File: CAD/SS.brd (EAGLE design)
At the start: 77 x 109 mm, 82 parts, among them Q1 SN74AHC-OR, Q2 UMD5N, Q4 SN74AHC-OR, Q5 BFP460, Q6 L78L05, Q7 NCP553, T1 MMBTRA104SS

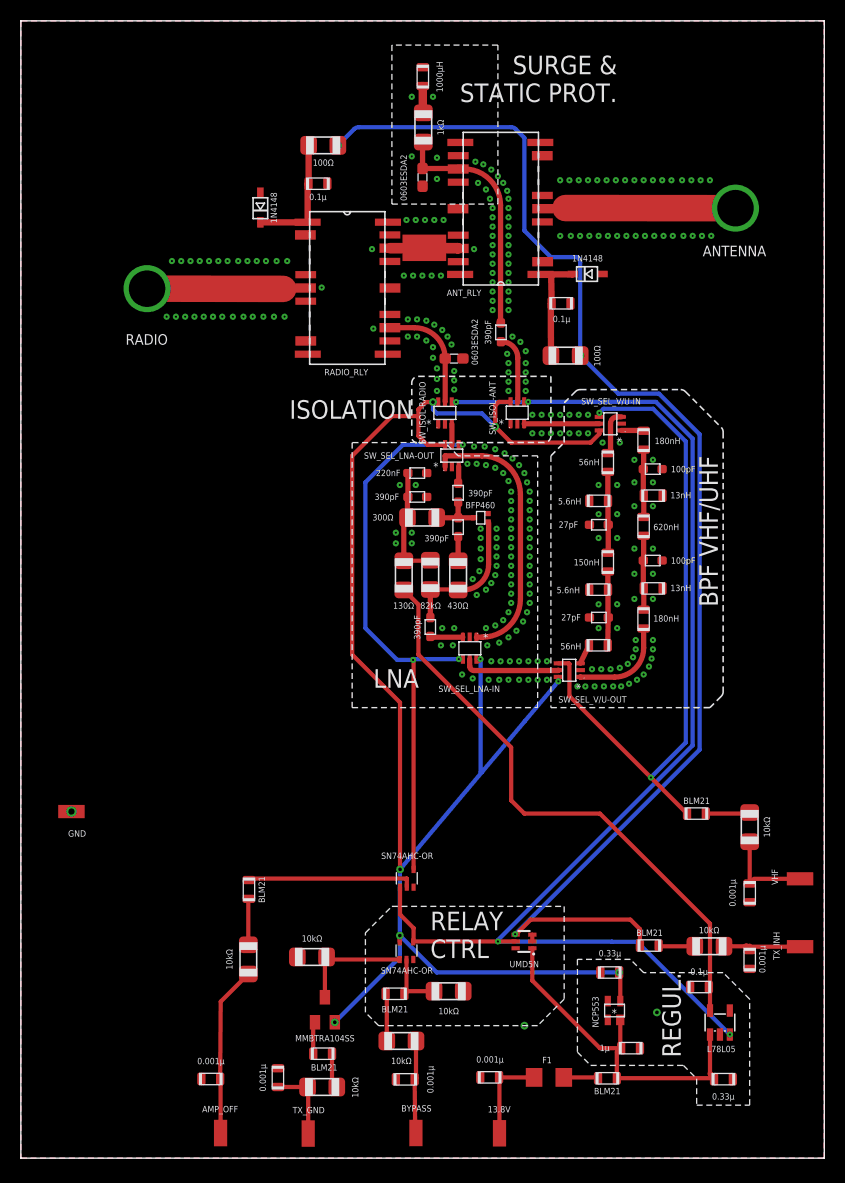
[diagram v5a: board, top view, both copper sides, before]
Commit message: Fixed relay/switch logics
* REviewed thoroughly the relay logic and connectors.
* Had to add a new "NOR" part. Complexity wins...
* Re-routed 5V regulator Enable pin to LNA logic
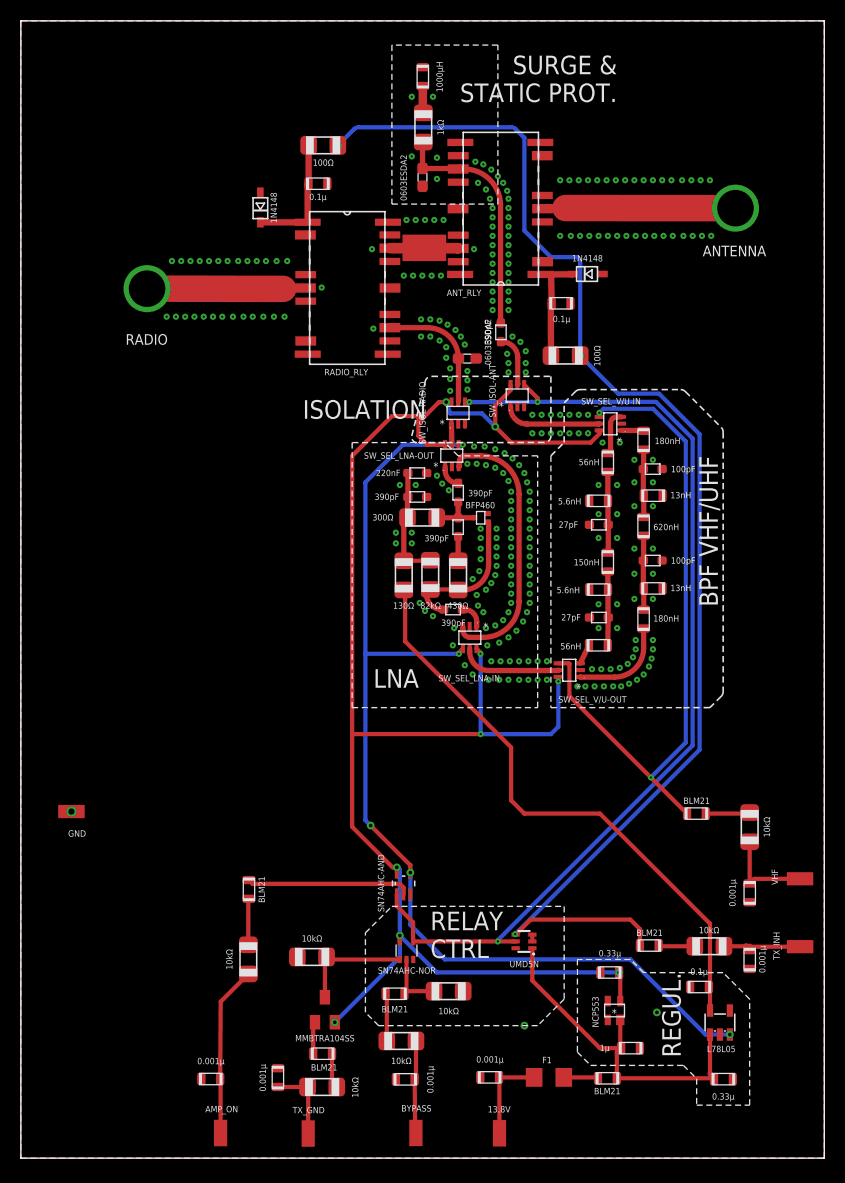
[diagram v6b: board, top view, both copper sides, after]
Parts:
- AMP_ON: value AMP_OFF -> AMP_ON
- Q1: value SN74AHC-OR -> SN74AHC-NOR
- Q4: value SN74AHC-OR -> SN74AHC-AND; device aarf:SC70-5 -> aarf:DCK5
- moved C8 2.75 mm to (41.4, 52.6), turned to 180 degrees
- moved SW_ISOL-ANT 1.65 mm to (47.6, 73.1)
- moved SW_ISOL-RADIO 1.27 mm to (41.9, 71.4)
- moved D4 1.27 mm to (42.8, 76.6)
- moved SW_SEL_LNA-IN 1.02 mm to (43.0, 49.9)
- moved Q4 0.59 mm to (36.7, 26.3), turned to 90 degrees
- renumbered AMP_OFF to AMP_ON
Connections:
- net AMP_OFF renamed AMP_ON
- net EXT_BYPASS renamed FORCE_BYPASS
- net RELAY_PWR renamed RELAY-RX_ON
- removed net LNA_OFF: Q4.4, SW_SEL_LNA-IN.4, SW_SEL_LNA-OUT.4
- removed net N$4: C8.P$1, SW_SEL_LNA-IN.3
- removed net RLY_BYPASS: Q1.4, Q2.5, Q4.1, Q6.3, SW_ISOL-ANT.4, SW_ISOL-RADIO.4
- new net BPF_ON: Q1.4, Q2.5, Q4.1, SW_ISOL-ANT.4, SW_ISOL-RADIO.4
- new net LNA_ON: Q4.4, Q6.3, SW_SEL_LNA-IN.4, SW_SEL_LNA-OUT.4
- new net N$3: C8.P$1, SW_SEL_LNA-IN.1
- net BPF_IN: now also SW_ISOL-ANT.1; no longer SW_ISOL-ANT.3
- net GND: now also SW_ISOL-ANT.3, SW_ISOL-RADIO.3; no longer SW_ISOL-ANT.1, SW_ISOL-RADIO.1
- net LNA-BYPASS: now also SW_SEL_LNA-IN.3, SW_SEL_LNA-OUT.3; no longer SW_SEL_LNA-IN.1, SW_SEL_LNA-OUT.1
- net LNA-SW_OUT: now also SW_ISOL-RADIO.1; no longer SW_ISOL-RADIO.3
- net N$1: now also SW_SEL_LNA-OUT.1; no longer SW_SEL_LNA-OUT.3
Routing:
- net RLY_BYPASS: track 122.5 -> 0.00 mm, vias 4 -> 0
- net LNA_ON: track 0.00 -> 100.0 mm, vias 0 -> 5
- net BPF_ON: track 0.00 -> 96.6 mm, vias 0 -> 3
- net LNA_OFF: track 55.9 -> 0.00 mm, vias 3 -> 0
- net N$4: track 3.15 -> 0.00 mm
- net N$3: track 0.00 -> 2.33 mm
- net BPF_IN: track 7.22 -> 9.28 mm
- net IN_DECPL: track 6.50 -> 4.84 mm
- net AMP+BPF_OUT: track 10.7 -> 12.0 mm
- net 3V: track 158.1 -> 157.3 mm, vias 8 -> 9
- net GND: track 0.13 -> 0.00 mm, vias 296 -> 298

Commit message: Updates to Board & Schematics
Schematic: 
* Added pads for 3V and 5V
Board:
* Added signal direction on signal pads
* Added a lot of gimmicks
* Added exposed copper so I can try the effects of covering some RF-critical sections with copper tape
* Reviewed some component position
* More comments
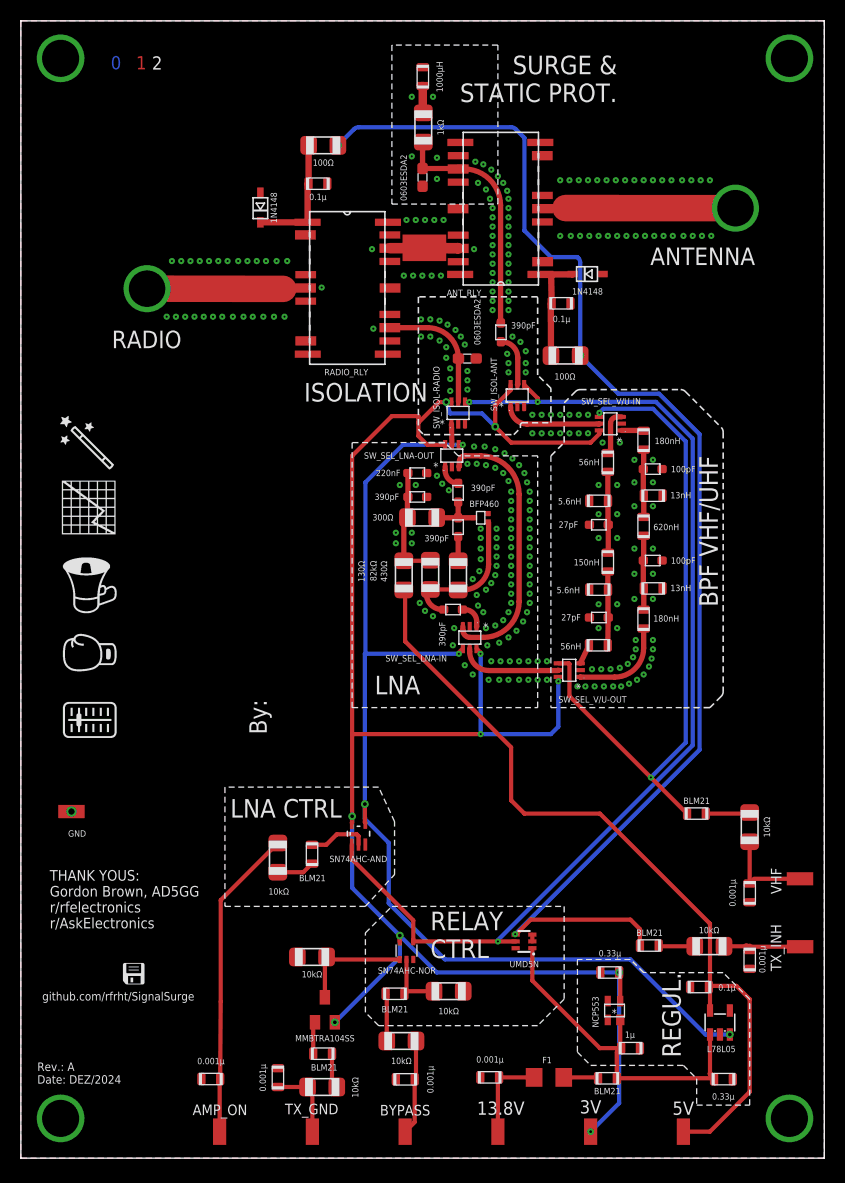
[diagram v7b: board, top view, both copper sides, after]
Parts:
- added 3V: 3V, wirepad:SMD1,27-2,54
- added 5V: 5V, wirepad:SMD1,27-2,54
- moved R12 10.2 mm to (24.6, 28.8), turned to 90 degrees
- moved FB6 6.93 mm to (27.9, 29.1)
- moved Q4 6.44 mm to (32.4, 31.1)
- moved BYPASS 1.04 mm to (36.8, 2.54)
- moved TX_GND 0.44 mm to (27.9, 2.54)
- moved 13.8V 0.22 mm to (45.7, 2.54)
- moved AMP_ON 0.16 mm to (19.1, 2.54)
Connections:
- net 3V: now also 3V.1
- net 5V: now also 5V.1
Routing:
- net 5V: track 56.8 -> 78.1 mm
- net 3V: track 157.3 -> 173.6 mm, vias 9 -> 10
- net N$15: track 16.4 -> 30.0 mm
- net AMP_ON: track 15.8 -> 5.76 mm
- net BPF_ON: track 96.6 -> 103.2 mm
- net LNA_ON: track 100.0 -> 101.9 mm, vias 5 -> 4
- net N$45: track 4.42 -> 3.61 mm
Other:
- board text added: "0"
- board text added: "1"
- board text added: "2"
- board text added: "3"
- board text added: "4"
- board text added: "By:"
- board text added: "LNA CTRL"
- board text added: "Rev.: A Date: DEZ/2024"
- board text added: "THANK YOUS: Gordon Brown, AD5GG r/rfelectronics r/AskElectronics"
- board text added: "github.com/rfrht/SignalSurge"

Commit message: SignalSurge: Several improvements (check comment for details)
* Changed the VHF BPF topology, using an impedance transformer to
  use a 1000 ohm-calculated BPF, yielding less critical component values
* Small improvements in BPF CPWs
* Implemented some changes suggested at r/rfElectronics
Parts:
- removed L5: 180nH, aarf:0805
- added C26: 22pF, aarf:GRM18
- added C27: 4.7pF, aarf:GRM18
- added C3, C5: 30pF, aarf:GRM18
- added C4: 390pF, aarf:GRM18
- C1: value 100pF -> 4.7pF
- C2: value 100pF -> 22pF
- L1: value 180nH -> 220nH
- L2: value 13nH -> 100nH
- L3: value 620nH -> 100nH
- L4: value 13nH -> 220nH
- moved L3 9.55 mm to (61.2, 51.1)
- moved C2 8.69 mm to (60.2, 66.0)
- moved L4 6.63 mm to (60.3, 48.0), turned to 180 degrees
- moved C1 3.73 mm to (60.3, 69.8)
- moved L2 3.59 mm to (61.1, 59.9), turned to 270 degrees
- moved L1 1.05 mm to (60.3, 67.9), turned to 0 degrees
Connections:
- new net N$19: C5.P$2, L3.P$1
- new net N$4: C1.P$1, C2.P$1, C3.P$2, L1.P$2
- new net N$6: C4.P$1, C5.P$1, L2.P$2
- net GND: now also C2.P$2, C26.P$2, C4.P$2, L1.P$1; no longer C1.P$1, C2.P$1, L2.P$2
- net N$14: now also C26.P$1, C27.P$1; no longer C2.P$2, L5.P$1
- net N$5: now also C3.P$1; no longer C1.P$2, L1.P$2, L3.P$1
- net VHF-IN: now also C1.P$2; no longer L1.P$1
- net VHF-OUT: now also C27.P$2; no longer L5.P$2
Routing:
- net VHF-OUT: track 9.11 -> 2.48 mm
- net N$4: track 0.00 -> 5.45 mm
- net N$5: track 6.49 -> 1.68 mm
- net N$6: track 0.00 -> 3.47 mm
- net N$19: track 0.00 -> 1.77 mm
- net 3V: track 173.6 -> 172.5 mm
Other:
- board text added: "Rev.: A Date: JAN/2025"
- board text removed: "Rev.: A Date: DEZ/2024"
